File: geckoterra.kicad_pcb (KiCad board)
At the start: 2 copper layers, 50 x 50 mm, 24 parts, among them J1 Conn_WallSocket_Earth, J6 Conn_01x02, J7 Conn_01x02, J8 Conn_01x02, K1 SANYOU_SRD_Form_A, P1 Conn_WallPlug_Earth, Q1 2N3904, Q2 Q_NMOS_GDS, U1 PC817, U2 4N25

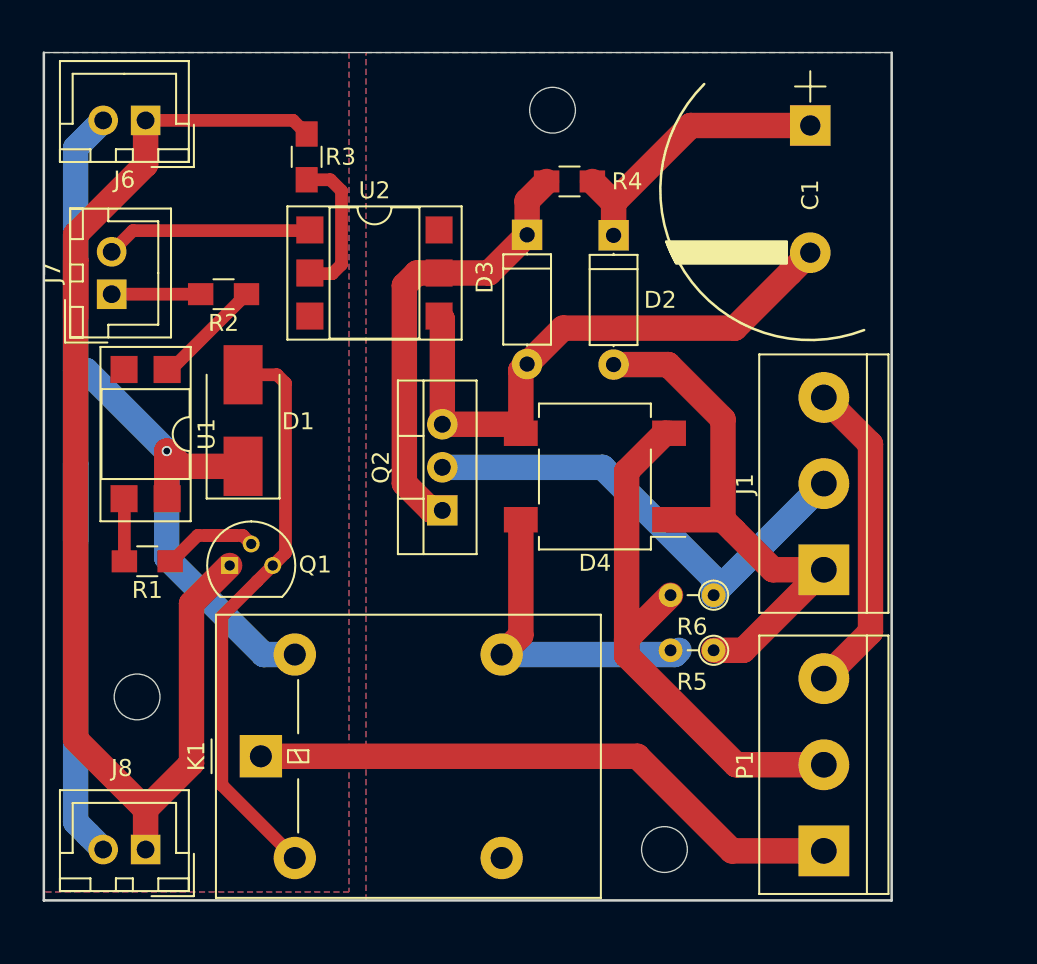
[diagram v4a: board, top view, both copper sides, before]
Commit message: Update to kicad5. Fix footprints. Move a bit to give size to the capacitor.
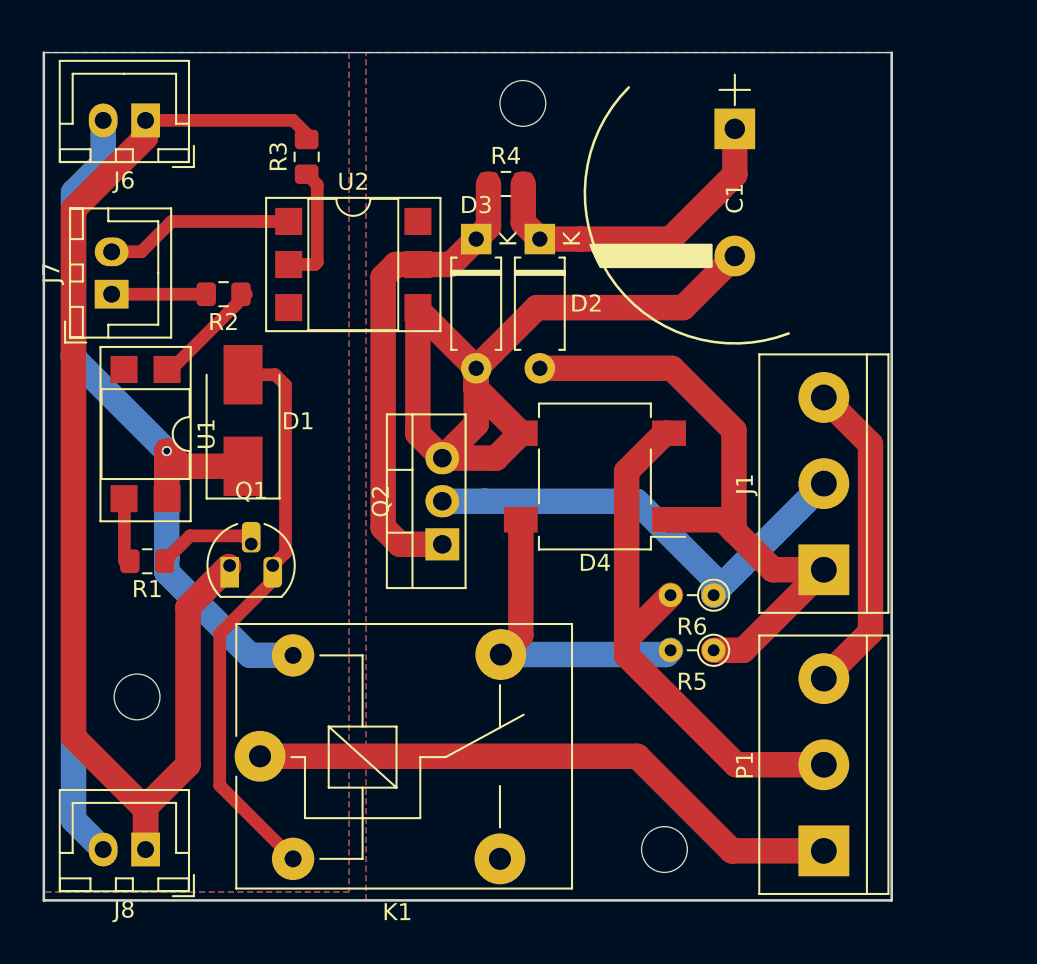
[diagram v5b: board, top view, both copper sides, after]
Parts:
- C1: value CP -> 100u
- D1: footprint Diodes_SMD:D_SMB_Handsoldering -> Diode_SMD:D_SMB_Handsoldering
- D2, D3: footprint Diodes_THT:D_A-405_P7.62mm_Horizontal -> Diode_THT:D_A-405_P7.62mm_Horizontal
- D4: footprint Diodes_SMD:Diode_Bridge_DFS -> Diode_SMD:Diode_Bridge_Vishay_DFS
- J1: value Conn_WallSocket_Earth -> AC_Output; footprint Connectors_Terminal_Blocks:TerminalBlock_bornier-3_P5.08mm -> TerminalBlock:TerminalBlock_bornier-3_P5.08mm
- J6, J7, J8: footprint Connectors_JST:JST_XH_B02B-XH-A_02x2.50mm_Straight -> Connector_JST:JST_XH_B02B-XH-A_1x02_P2.50mm_Vertical
- K1: value SANYOU_SRD_Form_A -> SANYOU_SRD_Form_C; footprint Relays_THT:Relay_SPDT_OMRON-G5LE-1 -> Relay_THT:Relay_SPDT_SANYOU_SRD_Series_Form_C
- P1: value Conn_WallPlug_Earth -> AC_Input; footprint Connectors_Terminal_Blocks:TerminalBlock_bornier-3_P5.08mm -> TerminalBlock:TerminalBlock_bornier-3_P5.08mm
- Q1: footprint TO_SOT_Packages_THT:TO-92_Molded_Narrow -> Package_TO_SOT_THT:TO-92_HandSolder
- Q2: footprint TO_SOT_Packages_THT:TO-220-3_Vertical -> Package_TO_SOT_THT:TO-220-3_Vertical
- R1, R2, R3, R4: footprint Resistors_SMD:R_0805_HandSoldering -> Resistor_SMD:R_0805_2012Metric_Pad1.15x1.40mm_HandSolder
- R5, R6: footprint Resistors_THT:R_Axial_DIN0204_L3.6mm_D1.6mm_P2.54mm_Vertical -> Resistor_THT:R_Axial_DIN0204_L3.6mm_D1.6mm_P2.54mm_Vertical
- U1: footprint Housings_DIP:DIP-4_W7.62mm_SMDSocket_SmallPads -> Package_DIP:DIP-4_W7.62mm_SMDSocket_SmallPads
- U2: footprint Housings_DIP:DIP-6_W7.62mm_SMDSocket_SmallPads -> Package_DIP:DIP-6_W7.62mm_SMDSocket_SmallPads
- moved C1 4.45 mm to (90.8, 54.5)
- moved D2 4.36 mm to (79.2, 61.0)
- moved R4 3.75 mm to (77.2, 57.8)
- moved D3 3.01 mm to (75.5, 61.0)
- moved Q2 2.00 mm to (73.5, 79.0)
- moved SC1 1.80 mm to (78.2, 53.0)
- moved U2 1.35 mm to (68.2, 62.5)
- turned K1 to 0 degrees
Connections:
- K1 pad 3: (no net) -> Net-(K1-Pad3)
- U2 pad 3: (no net) -> Net-(U2-Pad3)
- U2 pad 6: (no net) -> Net-(U2-Pad6)
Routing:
- net Net-(C1-Pad2): track 35.0 -> 48.8 mm
- net Net-(D2-Pad2): track 34.1 -> 39.3 mm
- net +5V: track 80.2 -> 76.8 mm
- net Net-(C1-Pad1): track 17.2 -> 19.4 mm
- net Net-(D3-Pad1): track 26.8 -> 28.6 mm
- net Net-(Q1-Pad2): track 7.40 -> 5.93 mm
- net Net-(R3-Pad1): track 8.57 -> 7.19 mm
- net /PWMPin: track 12.4 -> 11.2 mm
- net GND: track 76.1 -> 75.1 mm
- net Net-(J1-Pad2): track 30.2 -> 29.3 mm
- net Net-(D4-Pad4): track 19.0 -> 18.5 mm
